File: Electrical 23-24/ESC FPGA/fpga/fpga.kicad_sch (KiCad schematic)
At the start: 0 parts

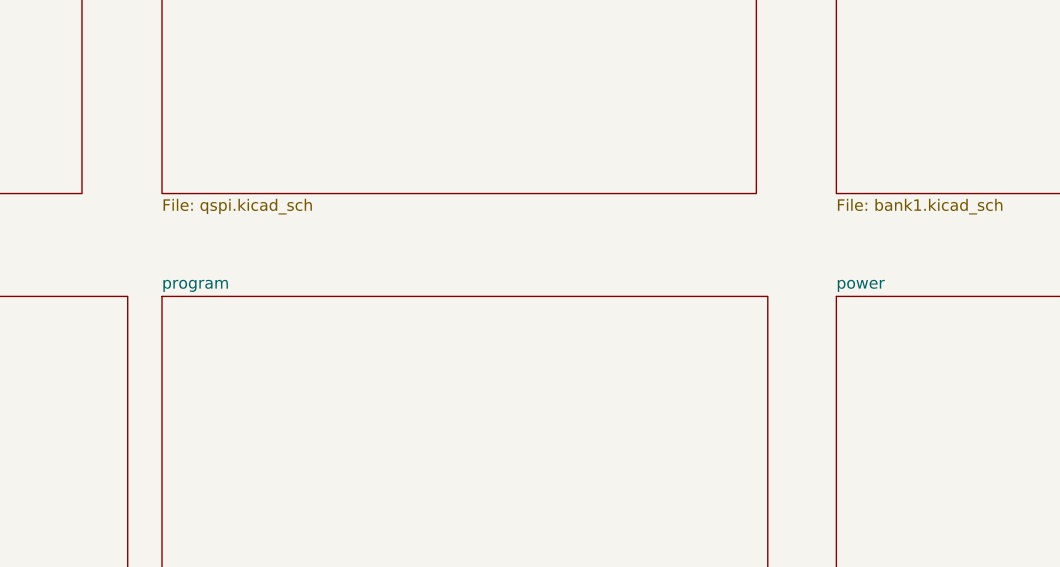
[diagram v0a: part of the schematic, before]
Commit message: Finish programming interface with FPGA
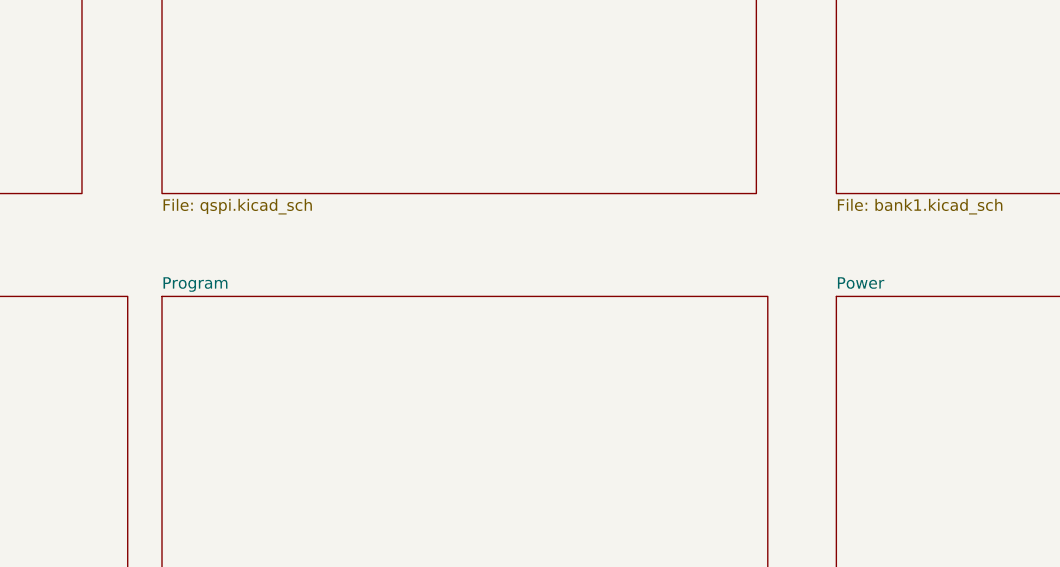
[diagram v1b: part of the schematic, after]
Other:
- sheet power renamed Power
- sheet program renamed Program
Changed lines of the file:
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@@
     (stroke (width 0.1524) (type solid))
     (fill (color 0 0 0 0.0000))
-    (property "Sheetname" "power" (at 165.1 76.7584 0)
+    (property "Sheetname" "Power" (at 165.1 76.7584 0)
       (effects (font (size 1.27 1.27)) (justify left bottom))
     )
@@
     (stroke (width 0.1524) (type solid))
     (fill (color 0 0 0 0.0000))
-    (property "Sheetname" "program" (at 90.17 76.7584 0)
+    (property "Sheetname" "Program" (at 90.17 76.7584 0)
       (effects (font (size 1.27 1.27)) (justify left bottom))
     )

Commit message: Add programmer
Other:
- added sheet JTAG (jtag.kicad_sch)
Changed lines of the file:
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@@
+    )
+  )
+  (sheet (at 90.17 130.81) (size 66.04 44.45) (fields_autoplaced)
+    (stroke (width 0.1524) (type solid))
+    (fill (color 0 0 0 0.0000))
+    (property "Sheetname" "JTAG" (at 90.17 130.0984 0)
+      (effects (font (size 1.27 1.27)) (justify left bottom))
+    )
+    (property "Sheetfile" "jtag.kicad_sch" (at 90.17 175.8446 0)
+      (effects (font (size 1.27 1.27)) (justify left top))
+    )
+    (instances
+      (project "fpga"
+        (path "/5bf59577-a814-4364-8f7a-37815cfb5474" (page "12"))
+      )
     )
   )

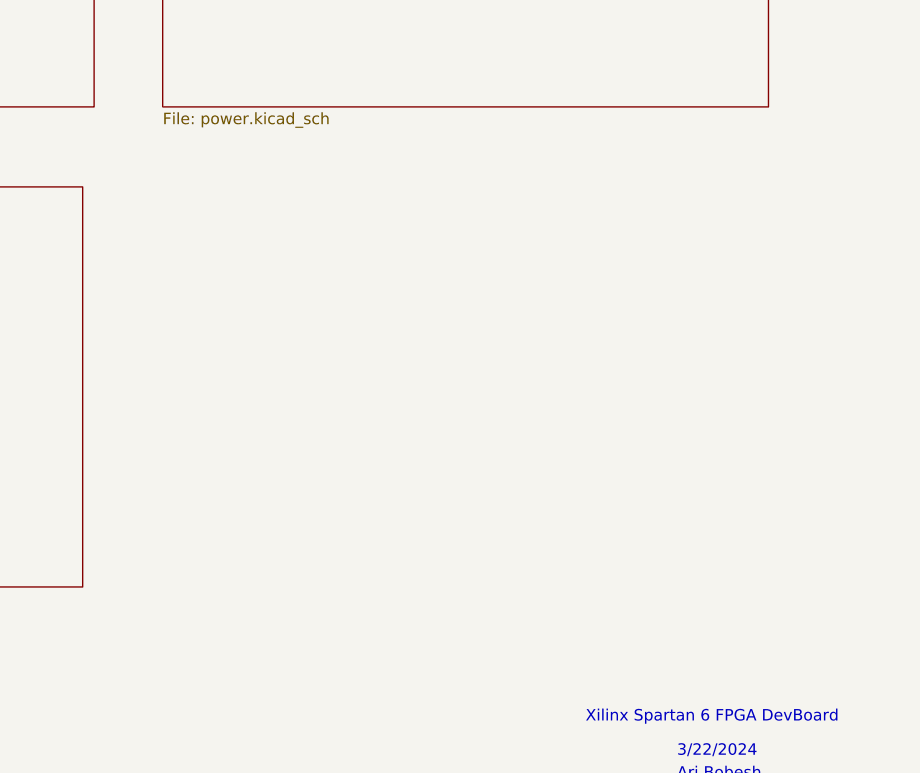
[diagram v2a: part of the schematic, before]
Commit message: Finished FPGA board schematic
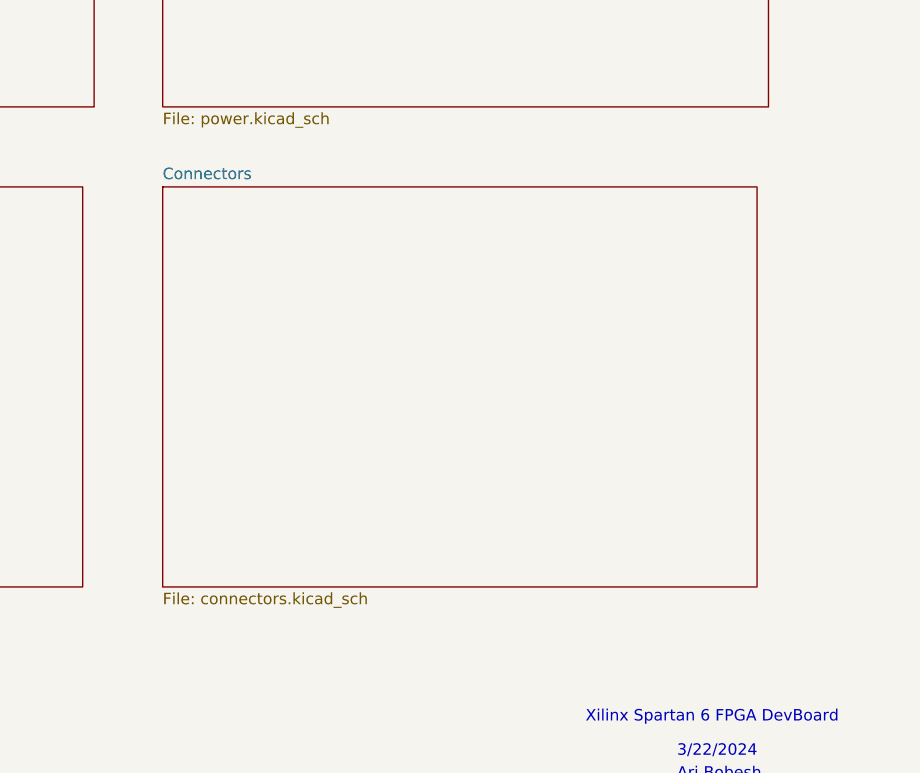
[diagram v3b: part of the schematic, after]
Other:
- added sheet Connectors (connectors.kicad_sch)
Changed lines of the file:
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@@
+    )
+  )
+  (sheet (at 165.1 130.81) (size 66.04 44.45) (fields_autoplaced)
+    (stroke (width 0.1524) (type solid))
+    (fill (color 0 0 0 0.0000))
+    (property "Sheetname" "Connectors" (at 165.1 130.0984 0)
+      (effects (font (size 1.27 1.27)) (justify left bottom))
+    )
+    (property "Sheetfile" "connectors.kicad_sch" (at 165.1 175.8446 0)
+      (effects (font (size 1.27 1.27)) (justify left top))
+    )
+    (instances
+      (project "fpga"
+        (path "/5bf59577-a814-4364-8f7a-37815cfb5474" (page "15"))
+      )
     )
   )
